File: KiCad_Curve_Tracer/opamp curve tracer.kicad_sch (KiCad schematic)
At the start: 10 parts, among them J1 Vi, J2 DUT, J3 rng, J4 Input, J5 Vo, U1 Opamp_Dual

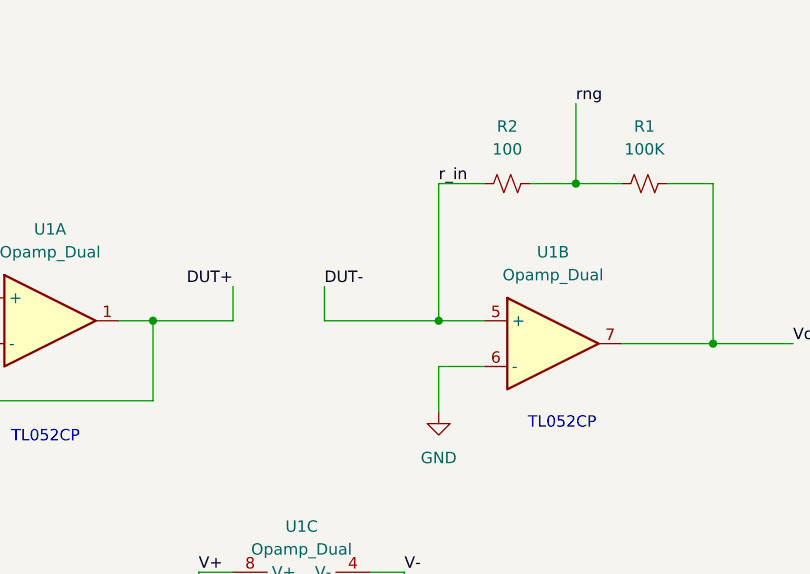
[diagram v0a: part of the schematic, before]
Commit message: Fixed the curve tracer PCB
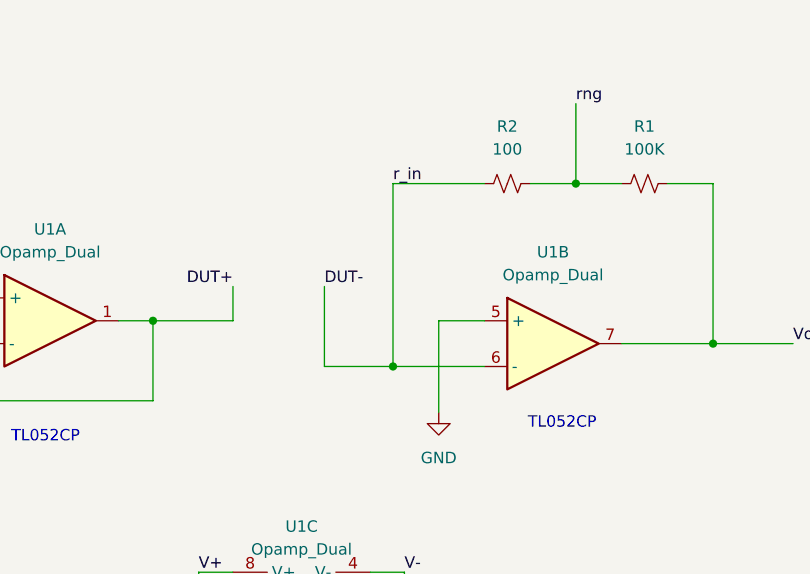
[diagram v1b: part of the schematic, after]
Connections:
- net DUT-: now also U1.6 (-); no longer U1.5 (+)
- net GND: now also U1.5 (+); no longer U1.6 (-)
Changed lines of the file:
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@@
 	(paper "A4")
+	(junction
+		(at 143.51 88.9)
+		(diameter 0)
+		(color 0 0 0 0)
+	)
 	(junction
 		(at 134.62 129.54)
@@
 	)
 	(junction
-		(at 148.59 83.82)
-		(diameter 0)
-		(color 0 0 0 0)
-	)
-	(junction
 		(at 179.07 86.36)
 		(diameter 0)
@@
 	(wire
 		(pts
-			(xy 148.59 68.58) (xy 153.67 68.58)
-		)
-		(stroke
-			(width 0)
-			(type default)
-		)
-	)
-	(wire
-		(pts
 			(xy 147.32 26.67) (xy 147.32 34.29)
 		)
@@
 	(wire
 		(pts
-			(xy 148.59 83.82) (xy 148.59 68.58)
-		)
-		(stroke
-			(width 0)
-			(type default)
-		)
-	)
-	(wire
-		(pts
 			(xy 121.92 111.76) (xy 125.73 111.76)
 		)
@@
 	(wire
 		(pts
-			(xy 148.59 83.82) (xy 135.89 83.82)
+			(xy 143.51 68.58) (xy 153.67 68.58)
+		)
+		(stroke
+			(width 0)
+			(type default)
+		)
+	)
+	(wire
+		(pts
+			(xy 143.51 88.9) (xy 135.89 88.9)
 		)
 		(stroke
@@
 	(wire
 		(pts
+			(xy 148.59 83.82) (xy 153.67 83.82)
+		)
+		(stroke
+			(width 0)
+			(type default)
+		)
+	)
+	(wire
+		(pts
 			(xy 116.84 83.82) (xy 116.84 92.71)
 		)
@@
 	(wire
 		(pts
-			(xy 153.67 83.82) (xy 148.59 83.82)
-		)
-		(stroke
-			(width 0)
-			(type default)
-		)
-	)
-	(wire
-		(pts
 			(xy 189.23 34.29) (xy 194.31 34.29)
 		)
@@
 	(wire
 		(pts
-			(xy 148.59 93.98) (xy 148.59 88.9)
+			(xy 148.59 83.82) (xy 148.59 93.98)
 		)
 		(stroke
@@
 	(wire
 		(pts
-			(xy 135.89 80.01) (xy 135.89 83.82)
+			(xy 135.89 80.01) (xy 135.89 88.9)
 		)
 		(stroke
@@
 	(wire
 		(pts
+			(xy 143.51 88.9) (xy 153.67 88.9)
+		)
+		(stroke
+			(width 0)
+			(type default)
+		)
+	)
+	(wire
+		(pts
 			(xy 173.99 26.67) (xy 173.99 34.29)
 		)
@@
 	(wire
 		(pts
+			(xy 143.51 68.58) (xy 143.51 88.9)
+		)
+		(stroke
+			(width 0)
+			(type default)
+		)
+	)
+	(wire
+		(pts
 			(xy 194.31 26.67) (xy 194.31 34.29)
 		)
@@
 		(pts
 			(xy 95.25 26.67) (xy 95.25 31.75)
-		)
-		(stroke
-			(width 0)
-			(type default)
-		)
-	)
-	(wire
-		(pts
-			(xy 148.59 88.9) (xy 153.67 88.9)
 		)
 		(stroke
@@
 	)
 	(label "r_in"
-		(at 148.59 68.58 0)
+		(at 143.51 68.58 0)
 		(fields_autoplaced yes)
 		(effects
